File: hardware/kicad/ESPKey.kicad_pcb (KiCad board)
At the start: 2 copper layers, 16 x 20 mm, 32 parts, among them P1 Power, P2 Wiegand, Q1 2N7002, Q2 2N7002, Q3 2N7002, U1 RT6212A/B, U2 ESP-12

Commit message: Remove unused component C3
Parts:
- removed C3: np, Capacitors_SMD:C_0402
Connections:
- U2 pad 15: (no net) -> unconnected-(U2-RXD-Pad15)
- U2 pad 16: (no net) -> unconnected-(U2-TXD-Pad16)
- U2 pad 2: (no net) -> unconnected-(U2-ADC-Pad2)
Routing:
- net Net-(U1-FB): track 3.86 -> 2.52 mm
- net +3V3: track 35.8 -> 35.3 mm

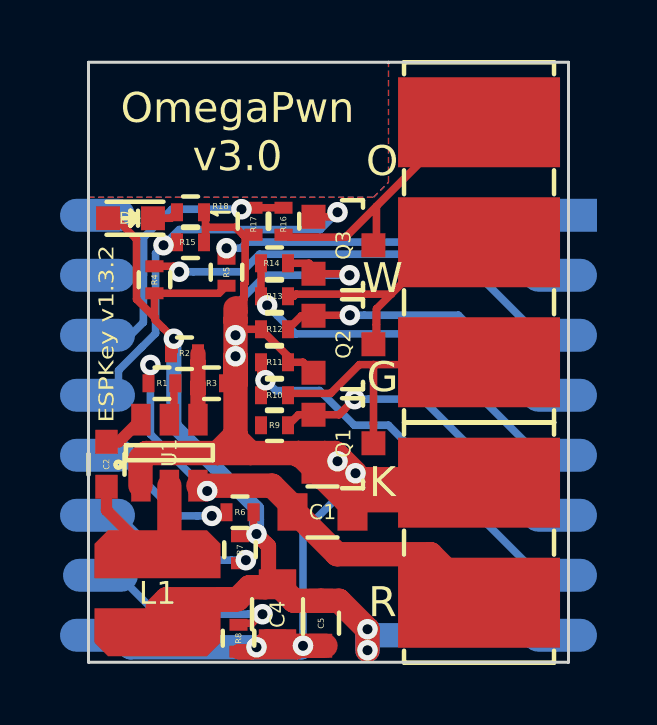
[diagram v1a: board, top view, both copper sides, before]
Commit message: Change footprint of R1, R2, R3 to 0603
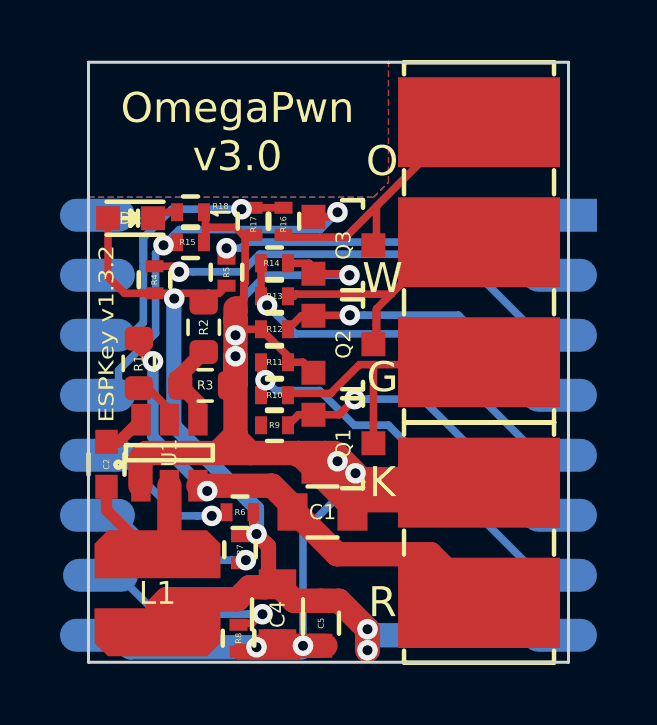
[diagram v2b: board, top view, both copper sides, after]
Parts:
- R1, R2, R3: footprint Resistors_SMD:R_0402 -> Resistor_SMD:R_0603_1608Metric
- moved R2 1.08 mm to (107.8, 108.8), turned to -90 degrees
- moved R1 1.02 mm to (105.7, 110.0), turned to 90 degrees
- moved R3 0.22 mm to (107.9, 110.8)
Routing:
- net +3V3: track 35.3 -> 34.3 mm

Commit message: Add OmegaPwn logo on back silkscreen
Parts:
- added G***: LOGO, OmegaPwn v3.0 Logo:Untitled, B.Cu at (112.0, 110.5)

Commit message: Update silkscreen for wiegand pads
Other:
- board text added: "+"
- board text added: "D0"
- board text added: "D1"
- board text added: "LED"
- board text removed: "G"
- board text removed: "K"
- board text removed: "O"
- board text removed: "R"
- board text removed: "W"
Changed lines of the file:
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@@
+	)
+	(gr_line
+		(start 113.425 114.4)
+		(end 114.225 114.4)
+		(stroke
+			(width 0.15)
+			(type default)
+		)
+		(layer "F.SilkS")
+	)
+	(gr_line
+		(start 113.725 114.9)
+		(end 113.95 114.9)
+		(stroke
+			(width 0.15)
+			(type default)
+		)
+		(layer "F.SilkS")
 	)
 	(gr_line
@@
 			(width 0.1)
 			(type solid)
+		)
+		(layer "F.SilkS")
+	)
+	(gr_line
+		(start 113.575 114.65)
+		(end 114.075 114.65)
+		(stroke
+			(width 0.15)
+			(type default)
+		)
+		(layer "F.SilkS")
+	)
+	(gr_line
+		(start 113.825 114.4)
+		(end 113.825 114)
+		(stroke
+			(width 0.15)
+			(type default)
 		)
 		(layer "F.SilkS")
@@
 		)
 	)
-	(gr_text "G"
-		(at 113.8 110.5 0)
+	(gr_text "D0"
+		(at 113.8 111.225 90)
 		(layer "F.SilkS")
 		(effects
 			(font
-				(size 1 1)
-				(thickness 0.2)
+				(size 0.7 0.7)
+				(thickness 0.175)
 			)
 		)
 	)
-	(gr_text "W"
-		(at 113.8 107.2 0)
+	(gr_text "D1"
+		(at 113.85 107.2 90)
 		(layer "F.SilkS")
 		(effects
 			(font
-				(size 1 1)
-				(thickness 0.2)
+				(size 0.7 0.7)
+				(thickness 0.175)
 			)
 		)
 	)
-	(gr_text "R"
+	(gr_text "+"
 		(at 113.8 118 0)
 		(layer "F.SilkS")
@@
 		)
 	)
-	(gr_text "K"
-		(at 113.8 114 0)
+	(gr_text "LED"
+		(at 113.825 103.175 90)
 		(layer "F.SilkS")
 		(effects
 			(font
-				(size 1 1)
-				(thickness 0.2)
+				(size 0.7 0.7)
+				(thickness 0.175)
 			)
 		)
-	)
-	(gr_text "O"
-		(at 113.787515 103.296817 0)
-		(layer "F.SilkS")
-		(effects
-			(font
-				(size 1 1)
-				(thickness 0.2)
-			)
-		)

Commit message: Adjust logo location on back silkscreen
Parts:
- moved G*** 0.50 mm to (112.0, 110.0)
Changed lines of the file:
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@@
 	(footprint "OmegaPwn v3.0 Logo:Untitled"
 		(layer "B.Cu")
-		(at 112 110.5 -90)
+		(at 112.05 110 -90)
 		(property "Reference" "G***"
 			(at 0 0 90)

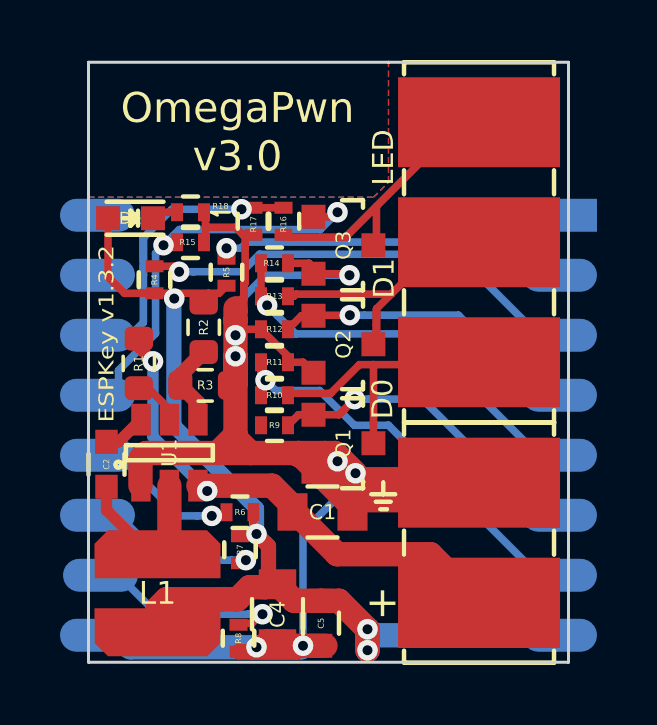
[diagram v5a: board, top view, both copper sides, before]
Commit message: Revert "Change footprint of R1, R2, R3 to 0603"
This reverts commit 8d4f8e3b
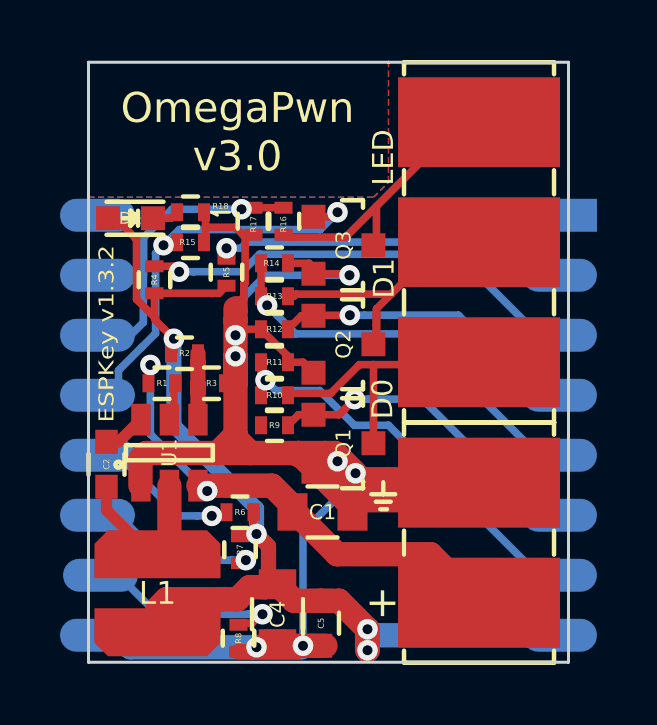
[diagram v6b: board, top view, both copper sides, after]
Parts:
- R1, R2, R3: footprint Resistor_SMD:R_0603_1608Metric -> Resistors_SMD:R_0402
- moved R2 1.08 mm to (107.2, 109.7), turned to 0 degrees
- moved R1 1.02 mm to (106.5, 110.7), turned to 180 degrees
- moved R3 0.22 mm to (108.1, 110.7)
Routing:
- net +3V3: track 34.3 -> 35.3 mm

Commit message: Revert R1, R2, R3 to 0402 and C3
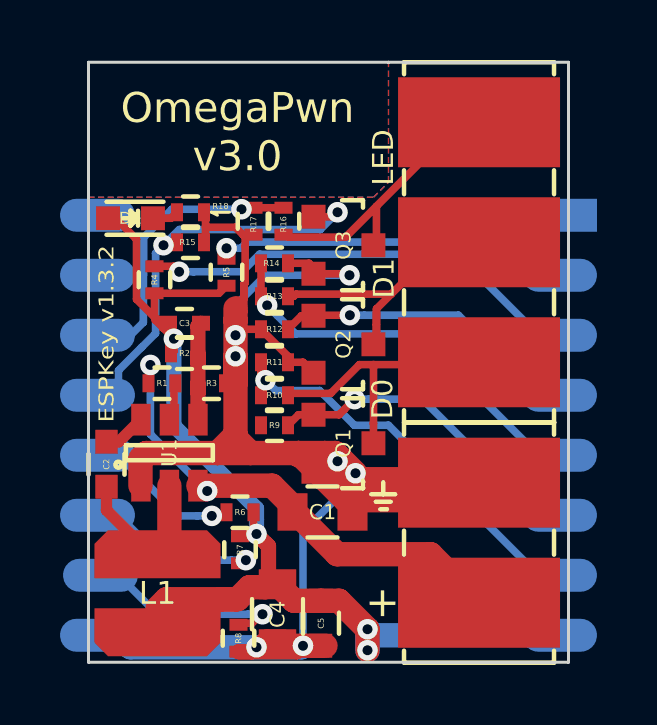
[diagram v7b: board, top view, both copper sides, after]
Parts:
- added C3: np, Capacitors_SMD:C_0402, F.Cu at (107.2, 108.7)
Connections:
- U2 pad 15: unconnected-(U2-RXD-Pad15) -> (no net)
- U2 pad 16: unconnected-(U2-TXD-Pad16) -> (no net)
- U2 pad 2: unconnected-(U2-ADC-Pad2) -> (no net)
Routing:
- net Net-(C3-Pad1): track 2.52 -> 3.86 mm
- net +3V3: track 35.3 -> 35.8 mm
